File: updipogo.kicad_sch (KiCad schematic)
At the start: 12 parts, among them J1 USB_C_Receptacle_USB2.0, J2 1.27, J3 2.54, J4 Header, U1 CH340N

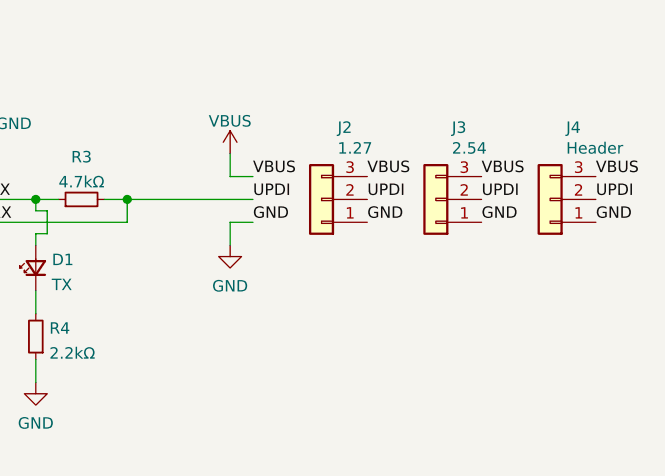
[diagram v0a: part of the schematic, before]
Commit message: change pinout of pogo pins to avoid rev. polarity danger
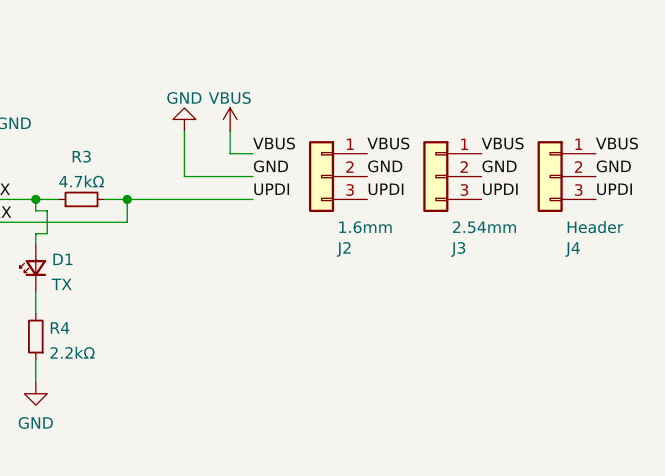
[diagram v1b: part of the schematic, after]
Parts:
- J2: value 1.27 -> 1.6mm; footprint local:PogoPins_1.27mm -> local:PogoPins_1.6mm
- J3: value 2.54 -> 2.54mm
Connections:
- net GND: now also J2.2 (Pin_2), J3.2 (Pin_2), J4.2 (Pin_2); no longer J2.1 (Pin_1), J3.1 (Pin_1), J4.1 (Pin_1)
- net RX: now also J2.3 (Pin_3), J3.3 (Pin_3), J4.3 (Pin_3); no longer J2.2 (Pin_2), J3.2 (Pin_2), J4.2 (Pin_2)
- net VBUS: now also J2.1 (Pin_1), J3.1 (Pin_1), J4.1 (Pin_1); no longer J2.3 (Pin_3), J3.3 (Pin_3), J4.3 (Pin_3)
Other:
- company: (none) -> ansemjo
- title: (none) -> updi pogo-pin programmer
- moved on the sheet: J2, J3, J4
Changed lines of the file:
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@@
 (kicad_sch (version 20210621) (generator eeschema)
-  (paper "A4")
+  (paper "A5")
+  (title_block
+    (title "updi pogo-pin programmer")
+    (date "2021-09-18")
+    (company "ansemjo")
+  )
   (junction (at 50.8 66.04) (diameter 1.016) (color 0 0 0 0))
   (junction (at 50.8 68.58) (diameter 1.016) (color 0 0 0 0))
@@
     (stroke (width 0) (type solid) (color 0 0 0 0))
   )
-  (wire (pts (xy 120.65 55.88) (xy 120.65 53.34))
-    (stroke (width 0) (type solid) (color 0 0 0 0))
-  )
-  (wire (pts (xy 120.65 55.88) (xy 123.19 55.88))
-    (stroke (width 0) (type solid) (color 0 0 0 0))
-  )
-  (wire (pts (xy 120.65 60.96) (xy 120.65 63.5))
-    (stroke (width 0) (type solid) (color 0 0 0 0))
-  )
-  (wire (pts (xy 120.65 60.96) (xy 123.19 60.96))
+  (wire (pts (xy 115.57 50.8) (xy 115.57 55.88))
+    (stroke (width 0) (type default) (color 0 0 0 0))
+  )
+  (wire (pts (xy 115.57 55.88) (xy 123.19 55.88))
+    (stroke (width 0) (type default) (color 0 0 0 0))
+  )
+  (wire (pts (xy 120.65 53.34) (xy 120.65 50.8))
+    (stroke (width 0) (type solid) (color 0 0 0 0))
+  )
+  (wire (pts (xy 120.65 53.34) (xy 123.19 53.34))
     (stroke (width 0) (type solid) (color 0 0 0 0))
   )
@@
     (effects (font (size 1.27 1.27)) (justify left bottom))
   )
-  (label "VBUS" (at 123.19 55.88 0)
+  (label "VBUS" (at 123.19 53.34 0)
+    (effects (font (size 1.27 1.27)) (justify left bottom))
+  )
+  (label "GND" (at 123.19 55.88 0)
     (effects (font (size 1.27 1.27)) (justify left bottom))
   )
@@
     (effects (font (size 1.27 1.27)) (justify left bottom))
   )
-  (label "GND" (at 123.19 60.96 0)
-    (effects (font (size 1.27 1.27)) (justify left bottom))
-  )
-  (label "VBUS" (at 135.89 55.88 0)
+  (label "VBUS" (at 135.89 53.34 0)
+    (effects (font (size 1.27 1.27)) (justify left bottom))
+  )
+  (label "GND" (at 135.89 55.88 0)
     (effects (font (size 1.27 1.27)) (justify left bottom))
   )
@@
     (effects (font (size 1.27 1.27)) (justify left bottom))
   )
-  (label "GND" (at 135.89 60.96 0)
-    (effects (font (size 1.27 1.27)) (justify left bottom))
-  )
-  (label "VBUS" (at 148.59 55.88 0)
+  (label "VBUS" (at 148.59 53.34 0)
+    (effects (font (size 1.27 1.27)) (justify left bottom))
+  )
+  (label "GND" (at 148.59 55.88 0)
     (effects (font (size 1.27 1.27)) (justify left bottom))
   )
@@
     (effects (font (size 1.27 1.27)) (justify left bottom))
   )
-  (label "GND" (at 148.59 60.96 0)
-    (effects (font (size 1.27 1.27)) (justify left bottom))
-  )
-  (label "VBUS" (at 161.29 55.88 0)
+  (label "VBUS" (at 161.29 53.34 0)
+    (effects (font (size 1.27 1.27)) (justify left bottom))
+  )
+  (label "GND" (at 161.29 55.88 0)
     (effects (font (size 1.27 1.27)) (justify left bottom))
   )
   (label "UPDI" (at 161.29 58.42 0)
-    (effects (font (size 1.27 1.27)) (justify left bottom))
-  )
-  (label "GND" (at 161.29 60.96 0)
     (effects (font (size 1.27 1.27)) (justify left bottom))
   )
@@
     (pin "1")
   )
-  (symbol (lib_id "power:VBUS") (at 120.65 53.34 0) (unit 1)
-    (in_bom yes) (on_board yes) (fields_autoplaced)
-    (property "Reference" "#PWR011" (id 0) (at 120.65 57.15 0)
-      (effects (font (size 1.27 1.27)) hide)
-    )
-    (property "Value" "VBUS" (id 1) (at 120.65 49.7354 0))
-    (property "Footprint" "" (id 2) (at 120.65 53.34 0)
-      (effects (font (size 1.27 1.27)) hide)
-    )
-    (property "Datasheet" "" (id 3) (at 120.65 53.34 0)
+  (symbol (lib_id "power:VBUS") (at 120.65 50.8 0) (unit 1)
+    (in_bom yes) (on_board yes) (fields_autoplaced)
+    (property "Reference" "#PWR011" (id 0) (at 120.65 54.61 0)
+      (effects (font (size 1.27 1.27)) hide)
+    )
+    (property "Value" "VBUS" (id 1) (at 120.65 47.1954 0))
+    (property "Footprint" "" (id 2) (at 120.65 50.8 0)
+      (effects (font (size 1.27 1.27)) hide)
+    )
+    (property "Datasheet" "" (id 3) (at 120.65 50.8 0)
       (effects (font (size 1.27 1.27)) hide)
     )
@@
     (pin "1")
   )
-  (symbol (lib_id "power:GND") (at 120.65 63.5 0) (unit 1)
-    (in_bom yes) (on_board yes) (fields_autoplaced)
-    (property "Reference" "#PWR012" (id 0) (at 120.65 69.85 0)
-      (effects (font (size 1.27 1.27)) hide)
-    )
-    (property "Value" "GND" (id 1) (at 120.65 68.0626 0))
-    (property "Footprint" "" (id 2) (at 120.65 63.5 0)
-      (effects (font (size 1.27 1.27)) hide)
-    )
-    (property "Datasheet" "" (id 3) (at 120.65 63.5 0)
+  (symbol (lib_id "power:GND") (at 115.57 50.8 180) (unit 1)
+    (in_bom yes) (on_board yes) (fields_autoplaced)
+    (property "Reference" "#PWR012" (id 0) (at 115.57 44.45 0)
+      (effects (font (size 1.27 1.27)) hide)
+    )
+    (property "Value" "GND" (id 1) (at 115.57 47.1954 0))
+    (property "Footprint" "" (id 2) (at 115.57 50.8 0)
+      (effects (font (size 1.27 1.27)) hide)
+    )
+    (property "Datasheet" "" (id 3) (at 115.57 50.8 0)
       (effects (font (size 1.27 1.27)) hide)
     )
@@
     (pin "2")
   )
-  (symbol (lib_id "Connector_Generic:Conn_01x03") (at 130.81 58.42 180) (unit 1)
+  (symbol (lib_id "Connector_Generic:Conn_01x03") (at 130.81 55.88 0) (mirror y) (unit 1)
     (in_bom yes) (on_board yes)
-    (property "Reference" "J2" (id 0) (at 132.5879 50.4385 0)
-      (effects (font (size 1.27 1.27)) (justify right))
-    )
-    (property "Value" "1.27" (id 1) (at 132.5879 52.7434 0)
-      (effects (font (size 1.27 1.27)) (justify right))
-    )
-    (property "Footprint" "local:PogoPins_1.27mm" (id 2) (at 130.81 58.42 0)
-      (effects (font (size 1.27 1.27)) hide)
-    )
-    (property "Datasheet" "~" (id 3) (at 130.81 58.42 0)
+    (property "Reference" "J2" (id 0) (at 132.5879 63.8615 0)
+      (effects (font (size 1.27 1.27)) (justify right))
+    )
+    (property "Value" "1.6mm" (id 1) (at 132.5879 61.5566 0)
+      (effects (font (size 1.27 1.27)) (justify right))
+    )
+    (property "Footprint" "local:PogoPins_1.6mm" (id 2) (at 130.81 55.88 0)
+      (effects (font (size 1.27 1.27)) hide)
+    )
+    (property "Datasheet" "~" (id 3) (at 130.81 55.88 0)
       (effects (font (size 1.27 1.27)) hide)
     )
@@
     (pin "3")
   )
-  (symbol (lib_id "Connector_Generic:Conn_01x03") (at 143.51 58.42 180) (unit 1)
+  (symbol (lib_id "Connector_Generic:Conn_01x03") (at 143.51 55.88 0) (mirror y) (unit 1)
     (in_bom yes) (on_board yes)
-    (property "Reference" "J3" (id 0) (at 145.2879 50.4385 0)
-      (effects (font (size 1.27 1.27)) (justify right))
-    )
-    (property "Value" "2.54" (id 1) (at 145.2879 52.7434 0)
-      (effects (font (size 1.27 1.27)) (justify right))
-    )
-    (property "Footprint" "local:PogoPins_2.54mm" (id 2) (at 143.51 58.42 0)
-      (effects (font (size 1.27 1.27)) hide)
-    )
-    (property "Datasheet" "~" (id 3) (at 143.51 58.42 0)
+    (property "Reference" "J3" (id 0) (at 145.2879 63.8615 0)
+      (effects (font (size 1.27 1.27)) (justify right))
+    )
+    (property "Value" "2.54mm" (id 1) (at 145.2879 61.5566 0)
+      (effects (font (size 1.27 1.27)) (justify right))
+    )
+    (property "Footprint" "local:PogoPins_2.54mm" (id 2) (at 143.51 55.88 0)
+      (effects (font (size 1.27 1.27)) hide)
+    )
+    (property "Datasheet" "~" (id 3) (at 143.51 55.88 0)
       (effects (font (size 1.27 1.27)) hide)
     )
@@
     (pin "3")
   )
-  (symbol (lib_id "Connector_Generic:Conn_01x03") (at 156.21 58.42 180) (unit 1)
+  (symbol (lib_id "Connector_Generic:Conn_01x03") (at 156.21 55.88 0) (mirror y) (unit 1)
     (in_bom yes) (on_board yes)
-    (property "Reference" "J4" (id 0) (at 157.9879 50.4385 0)
-      (effects (font (size 1.27 1.27)) (justify right))
-    )
-    (property "Value" "Header" (id 1) (at 157.9879 52.7434 0)
-      (effects (font (size 1.27 1.27)) (justify right))
-    )
-    (property "Footprint" "local:CustomPinHeader_1x03_P2.54mm_Horizontal" (id 2) (at 156.21 58.42 0)
-      (effects (font (size 1.27 1.27)) hide)
-    )
-    (property "Datasheet" "~" (id 3) (at 156.21 58.42 0)
+    (property "Reference" "J4" (id 0) (at 157.9879 63.8615 0)
+      (effects (font (size 1.27 1.27)) (justify right))
+    )
+    (property "Value" "Header" (id 1) (at 157.9879 61.5566 0)
+      (effects (font (size 1.27 1.27)) (justify right))
+    )
+    (property "Footprint" "local:CustomPinHeader_1x03_P2.54mm_Horizontal" (id 2) (at 156.21 55.88 0)
+      (effects (font (size 1.27 1.27)) hide)
+    )
+    (property "Datasheet" "~" (id 3) (at 156.21 55.88 0)
       (effects (font (size 1.27 1.27)) hide)
     )
@@
     )
     (path "/351a17bd-a44b-48ce-b198-6560a074af1e"
-      (reference "J2") (unit 1) (value "1.27") (footprint "local:PogoPins_1.27mm")
+      (reference "J2") (unit 1) (value "1.6mm") (footprint "local:PogoPins_1.6mm")
     )
     (path "/2af42b05-8567-4250-9ddc-6322e80b3448"
-      (reference "J3") (unit 1) (value "2.54") (footprint "local:PogoPins_2.54mm")
+      (reference "J3") (unit 1) (value "2.54mm") (footprint "local:PogoPins_2.54mm")
     )
     (path "/0e9ce192-f7c0-430b-a80d-540bfc73c3c3"

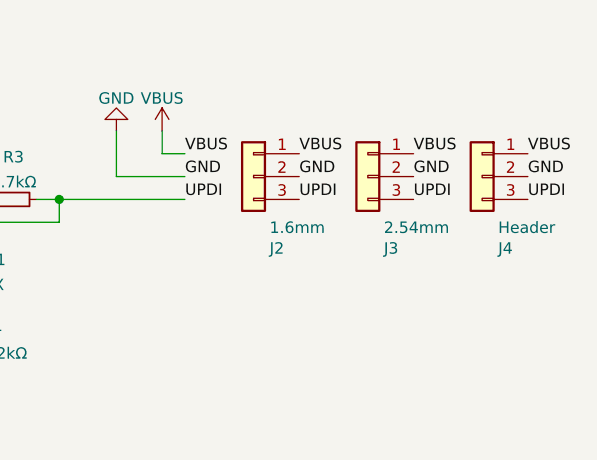
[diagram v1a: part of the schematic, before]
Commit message: reverse pin numbering and add footprint for pads
updi pin is now pin 1 and is square / boxed-in on programming pads
footprint
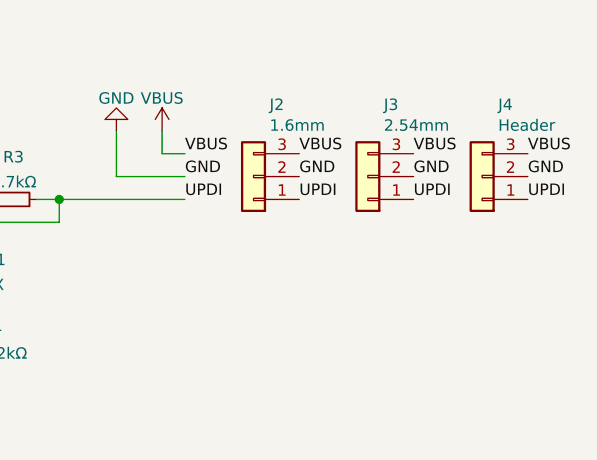
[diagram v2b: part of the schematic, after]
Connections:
- net RX: now also J2.1 (Pin_1), J3.1 (Pin_1), J4.1 (Pin_1); no longer J2.3 (Pin_3), J3.3 (Pin_3), J4.3 (Pin_3)
- net VBUS: now also J2.3 (Pin_3), J3.3 (Pin_3), J4.3 (Pin_3); no longer J2.1 (Pin_1), J3.1 (Pin_1), J4.1 (Pin_1)
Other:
- moved on the sheet: J2, J3, J4
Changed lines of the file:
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@@
     (pin "2")
   )
-  (symbol (lib_id "Connector_Generic:Conn_01x03") (at 130.81 55.88 0) (mirror y) (unit 1)
+  (symbol (lib_id "Connector_Generic:Conn_01x03") (at 130.81 55.88 180) (unit 1)
     (in_bom yes) (on_board yes)
-    (property "Reference" "J2" (id 0) (at 132.5879 63.8615 0)
+    (property "Reference" "J2" (id 0) (at 132.5879 47.8985 0)
       (effects (font (size 1.27 1.27)) (justify right))
     )
-    (property "Value" "1.6mm" (id 1) (at 132.5879 61.5566 0)
+    (property "Value" "1.6mm" (id 1) (at 132.5879 50.2034 0)
       (effects (font (size 1.27 1.27)) (justify right))
     )
@@
     (pin "3")
   )
-  (symbol (lib_id "Connector_Generic:Conn_01x03") (at 143.51 55.88 0) (mirror y) (unit 1)
+  (symbol (lib_id "Connector_Generic:Conn_01x03") (at 143.51 55.88 180) (unit 1)
     (in_bom yes) (on_board yes)
-    (property "Reference" "J3" (id 0) (at 145.2879 63.8615 0)
+    (property "Reference" "J3" (id 0) (at 145.2879 47.8985 0)
       (effects (font (size 1.27 1.27)) (justify right))
     )
-    (property "Value" "2.54mm" (id 1) (at 145.2879 61.5566 0)
+    (property "Value" "2.54mm" (id 1) (at 145.2879 50.2034 0)
       (effects (font (size 1.27 1.27)) (justify right))
     )
@@
     (pin "3")
   )
-  (symbol (lib_id "Connector_Generic:Conn_01x03") (at 156.21 55.88 0) (mirror y) (unit 1)
+  (symbol (lib_id "Connector_Generic:Conn_01x03") (at 156.21 55.88 180) (unit 1)
     (in_bom yes) (on_board yes)
-    (property "Reference" "J4" (id 0) (at 157.9879 63.8615 0)
+    (property "Reference" "J4" (id 0) (at 157.9879 47.8985 0)
       (effects (font (size 1.27 1.27)) (justify right))
     )
-    (property "Value" "Header" (id 1) (at 157.9879 61.5566 0)
+    (property "Value" "Header" (id 1) (at 157.9879 50.2034 0)
       (effects (font (size 1.27 1.27)) (justify right))
     )

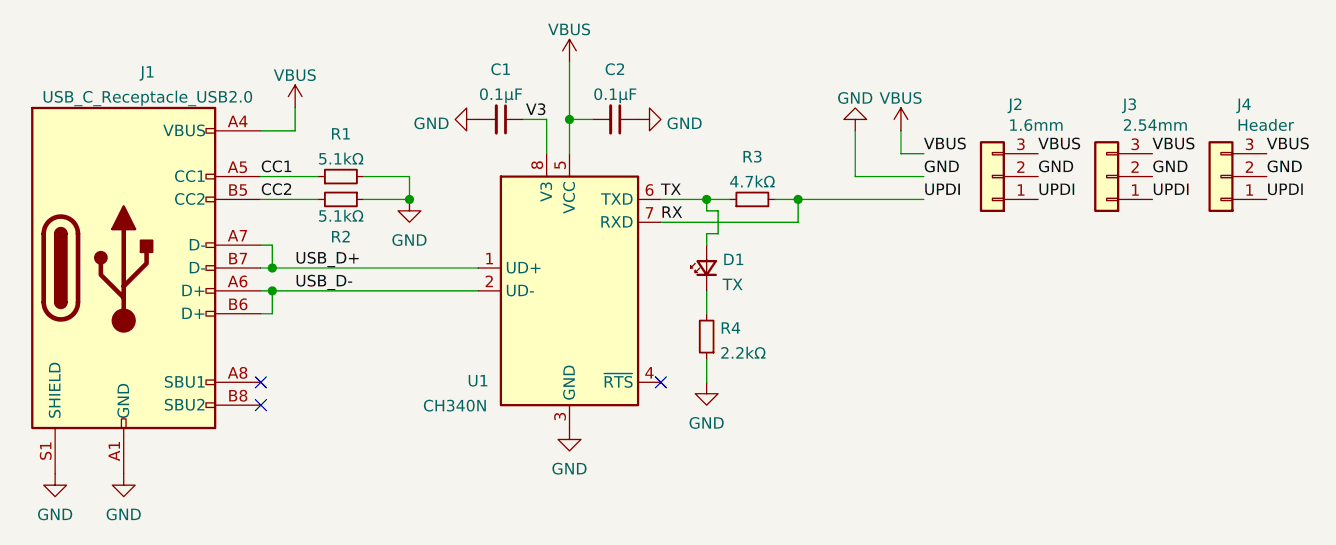
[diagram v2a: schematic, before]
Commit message: fix usb polarity
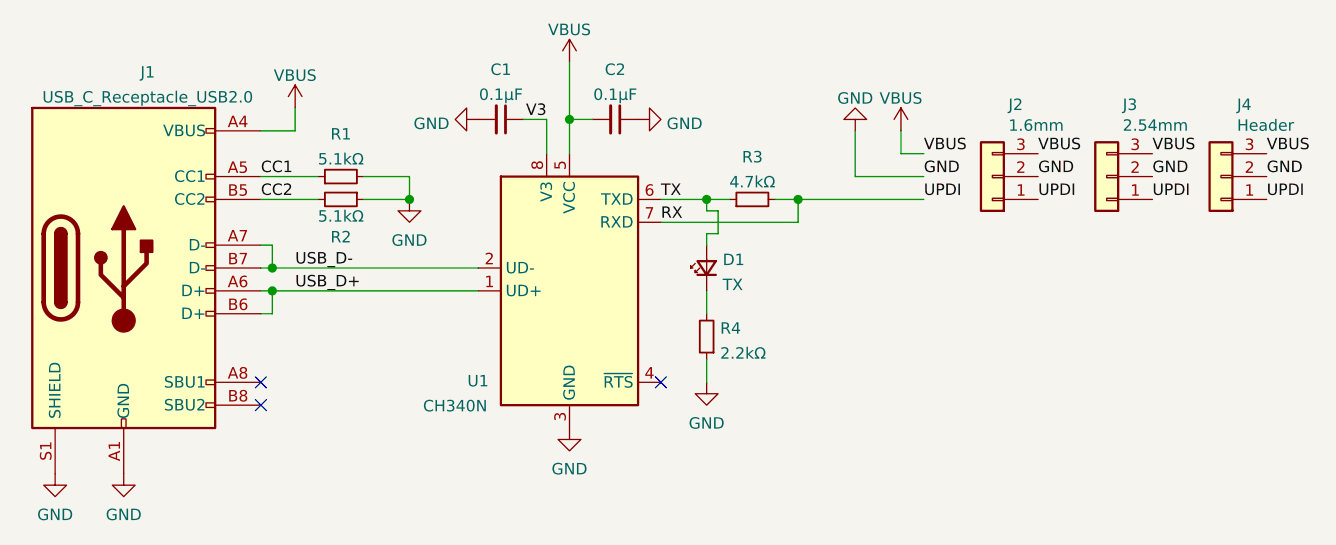
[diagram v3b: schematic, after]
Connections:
- net USB_D+: now also J1.A6 (D+), J1.B6 (D+); no longer J1.A7 (D-), J1.B7 (D-)
- net USB_D-: now also J1.A7 (D-), J1.B7 (D-); no longer J1.A6 (D+), J1.B6 (D+)
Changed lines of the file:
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@@
     (effects (font (size 1.27 1.27)) (justify left bottom))
   )
-  (label "USB_D+" (at 53.34 66.04 0)
+  (label "USB_D-" (at 53.34 66.04 0)
     (effects (font (size 1.27 1.27)) (justify left bottom))
   )
-  (label "USB_D-" (at 53.34 68.58 0)
+  (label "USB_D+" (at 53.34 68.58 0)
     (effects (font (size 1.27 1.27)) (justify left bottom))
   )

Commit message: connect led to RTS and update pcb layout a bit
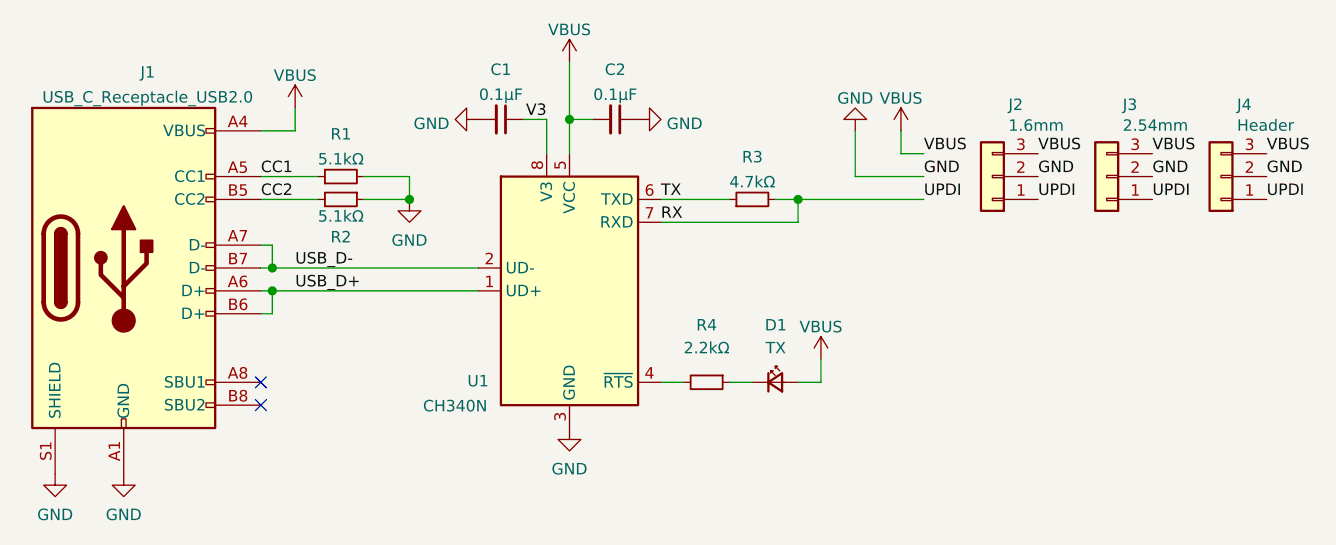
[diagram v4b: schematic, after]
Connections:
- net GND: no longer R4.1
- net TX: no longer D1.2 (A)
- net VBUS: now also D1.2 (A)
- net at D1.1 (K): now also R4.1; no longer R4.2
- net at U1.4 (~{RTS}): now also R4.2
- no-connect marks 3 -> 2
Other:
- moved on the sheet: D1, R4
